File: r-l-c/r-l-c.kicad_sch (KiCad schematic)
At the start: 2 parts

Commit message: r-l-c simulation ok
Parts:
- removed V1: 5, symbol Simulation_SPICE:VDC
- added C1: 10u, symbol Device:C
- added J1, J2: Conn_01x02_Pin, symbol Connector:Conn_01x02_Pin
- added L1: 10m, symbol Device:L
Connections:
- net at R1.1: now also J1.1 (Pin_1)
- net 0 renamed OUT
- net OUT: now also C1.1, J2.1 (Pin_1), L1.1
- new net GND: C1.2, J1.2 (Pin_2), J2.2 (Pin_2), L1.2

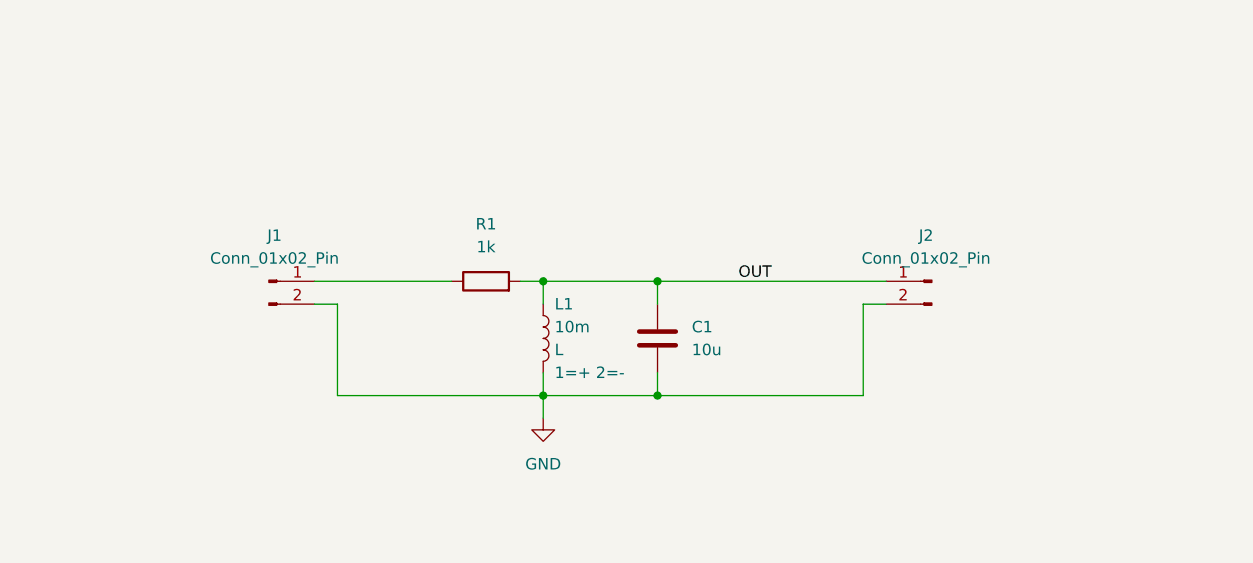
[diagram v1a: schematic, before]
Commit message: transistor switching working
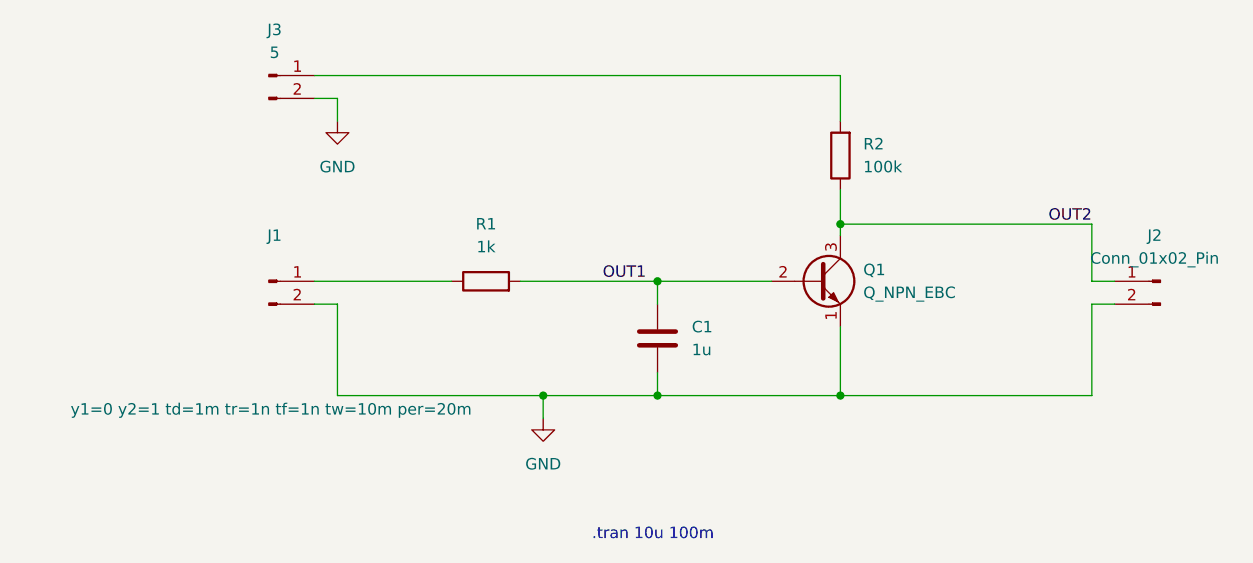
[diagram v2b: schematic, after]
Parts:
- removed L1: 10m, symbol Device:L
- added J3: 5, symbol Connector:Conn_01x02_Pin
- added Q1: Q_NPN_EBC, symbol Transistor_BJT:Q_NPN_EBC
- added R2: 100k, symbol Device:R
- C1: value 10u -> 1u
- J1: value Conn_01x02_Pin -> ${SIM.PARAMS}
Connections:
- net GND: now also J3.2 (Pin_2), Q1.1 (E)
- net OUT renamed OUT1
- net OUT1: now also Q1.2 (B); no longer J2.1 (Pin_1)
- new net: J3.1 (Pin_1), R2.2
- new net OUT2: J2.1 (Pin_1), Q1.3 (C), R2.1
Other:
- note added: ".tran 10u 100m"
- moved on the sheet: J2
